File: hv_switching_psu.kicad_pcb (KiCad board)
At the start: 2 copper layers, 53.3 x 85 mm, 22 parts, among them P1 CONN_2, P2 CONN_2, P3 CONN_2, P4 CONN_1, SW1 SWITCH_INV, T1 IRF644PBF, U1 MAX1771

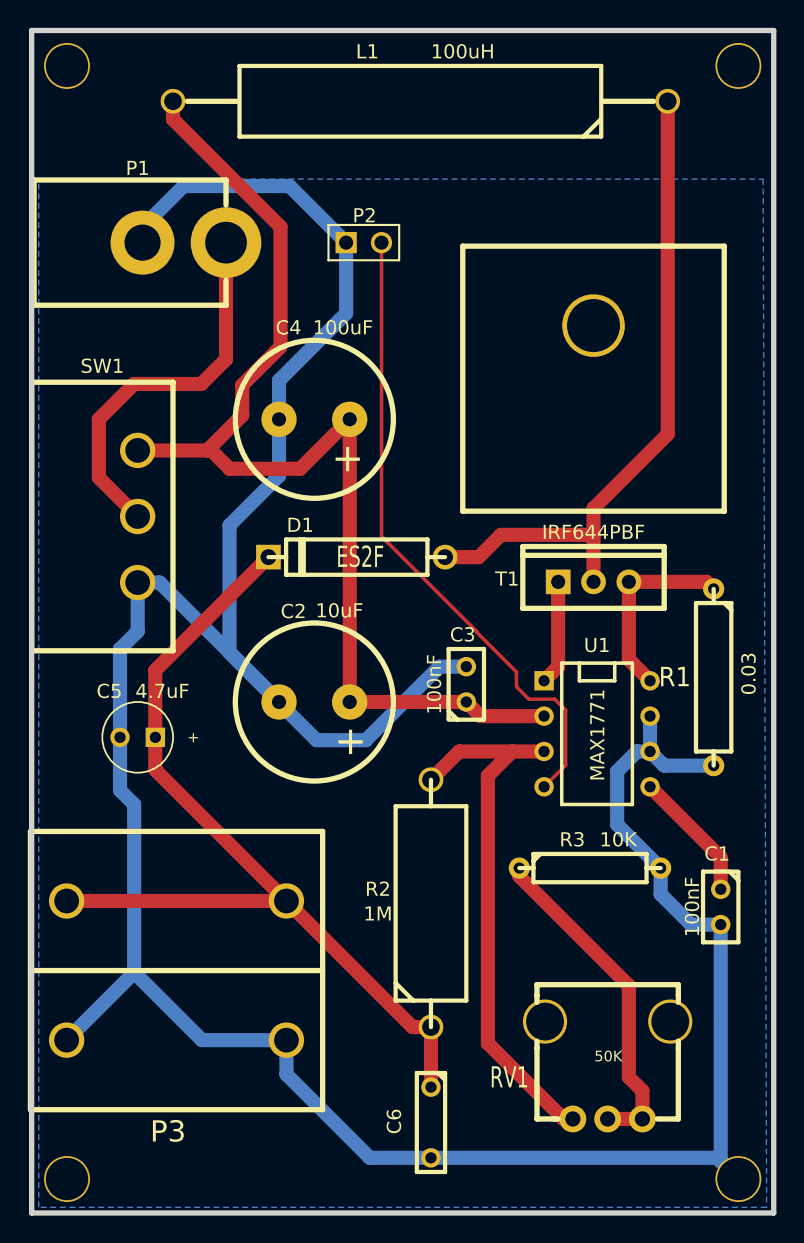
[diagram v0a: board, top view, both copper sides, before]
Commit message: Modified resistor settings.
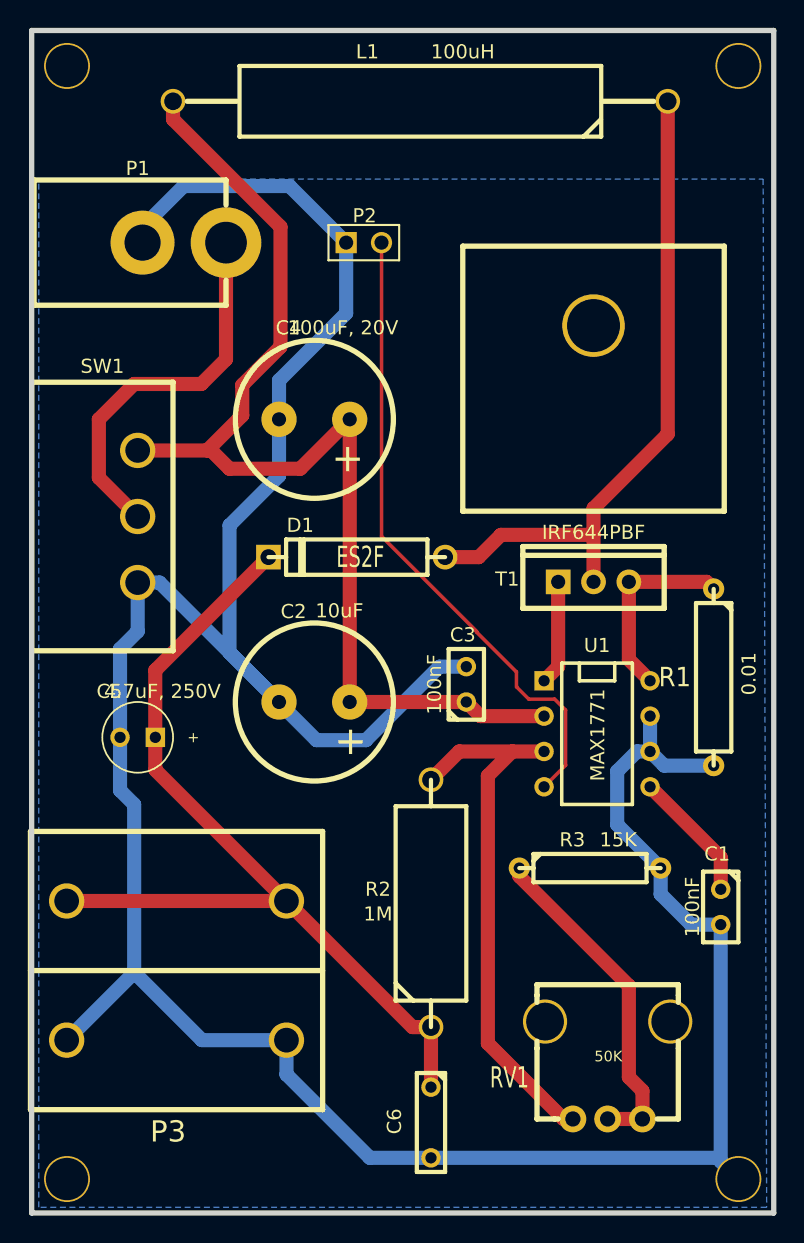
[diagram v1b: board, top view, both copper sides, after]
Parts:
- C4: value 100uF -> 100uF, 20V
- C5: value 4.7uF -> 4.7uF, 250V
- R1: value 0.03 -> 0.01
- R3: value 10K -> 15K
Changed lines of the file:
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@@
       (effects (font (size 1.016 1.016) (thickness 0.2032)))
     )
-    (fp_text value 100uF (at -2.0574 6.5786 180) (layer F.SilkS)
+    (fp_text value "100uF, 20V" (at -2.0574 6.5786 180) (layer F.SilkS)
       (effects (font (size 1.016 1.016) (thickness 0.2032)))
     )
@@
       (effects (font (size 1.016 1.016) (thickness 0.2032)))
     )
-    (fp_text value 4.7uF (at -1.778 3.302 180) (layer F.SilkS)
+    (fp_text value "4.7uF, 250V" (at -1.778 3.302 180) (layer F.SilkS)
       (effects (font (size 1.016 1.016) (thickness 0.2032)))
     )
@@
       (effects (font (size 1.016 1.016) (thickness 0.2032)))
     )
-    (fp_text value 10K (at 2.032 -2.032) (layer F.SilkS)
+    (fp_text value 15K (at 2.032 -2.032) (layer F.SilkS)
       (effects (font (size 1.016 1.016) (thickness 0.2032)))
     )
@@
       (effects (font (size 1.397 1.27) (thickness 0.2032)))
     )
-    (fp_text value 0.03 (at -0.254 -2.54 270) (layer F.SilkS)
-      (effects (font (size 1.016 1.016) (thickness 0.2032)))
-    )
+    (fp_text value 0.01 (at -0.254 -2.54 270) (layer F.SilkS)
+      (effects (font (size 1.016 1.016) (thickness 0.2032)))
+    )

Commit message: Added version 1.3 Gerber files.
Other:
- board text added: "IO Rodeo Inc. Electrophoresis Power Supply v 1.3"
- board text removed: "IO Rodeo Inc. Electrophoresis Power Supply v 1.2"
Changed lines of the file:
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@@
       (drillshape 0)
       (scaleselection 1)
-      (outputdirectory gerber_v1.2/))
+      (outputdirectory gerber_v1.3/))
   )
   (net 0 "")
@@
   (gr_line (start 139.7 165) (end 86.36 165) (angle 90) (layer Edge.Cuts) (width 0.381))
   (gr_line (start 86.36 80) (end 139.7 80) (angle 90) (layer Edge.Cuts) (width 0.381))
-  (gr_text "IO Rodeo Inc.\nElectrophoresis Power Supply v 1.2" (at 114.554 83.312) (layer B.SilkS)
+  (gr_text "IO Rodeo Inc.\nElectrophoresis Power Supply v 1.3" (at 114.554 83.312) (layer B.SilkS)
     (effects (font (size 1.524 1.016) (thickness 0.254)) (justify mirror))
   )

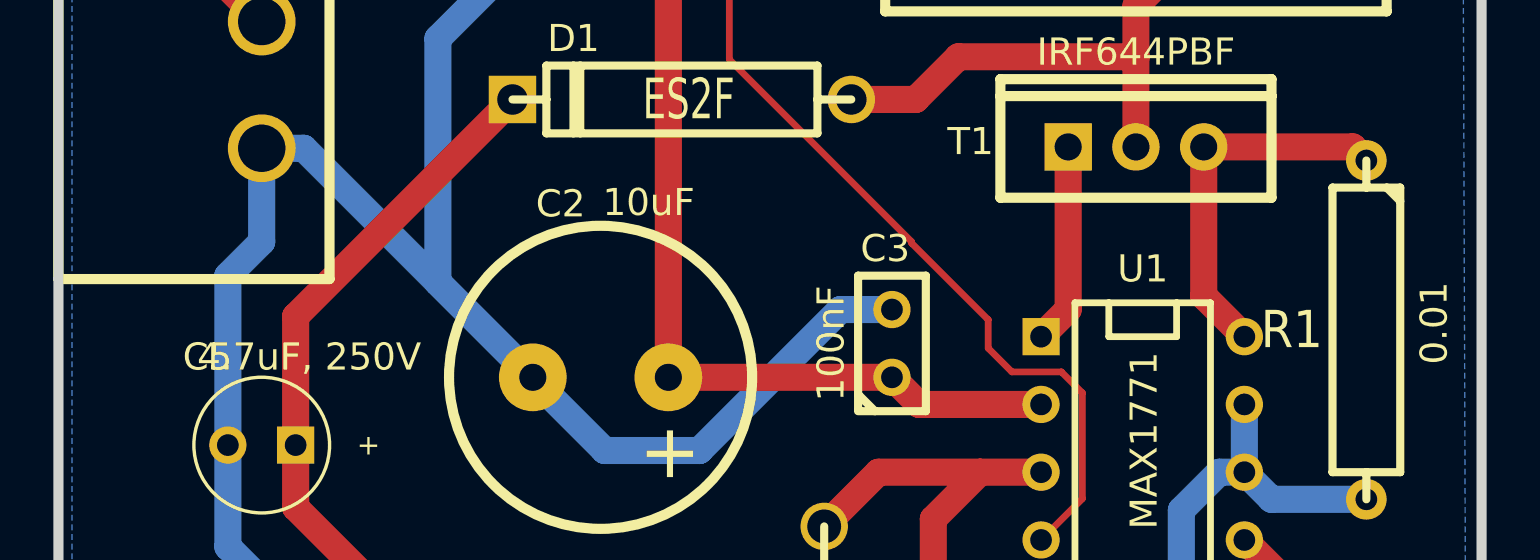
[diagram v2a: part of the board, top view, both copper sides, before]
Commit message: Modified silkscreen, remade v1.3 of gerber files.
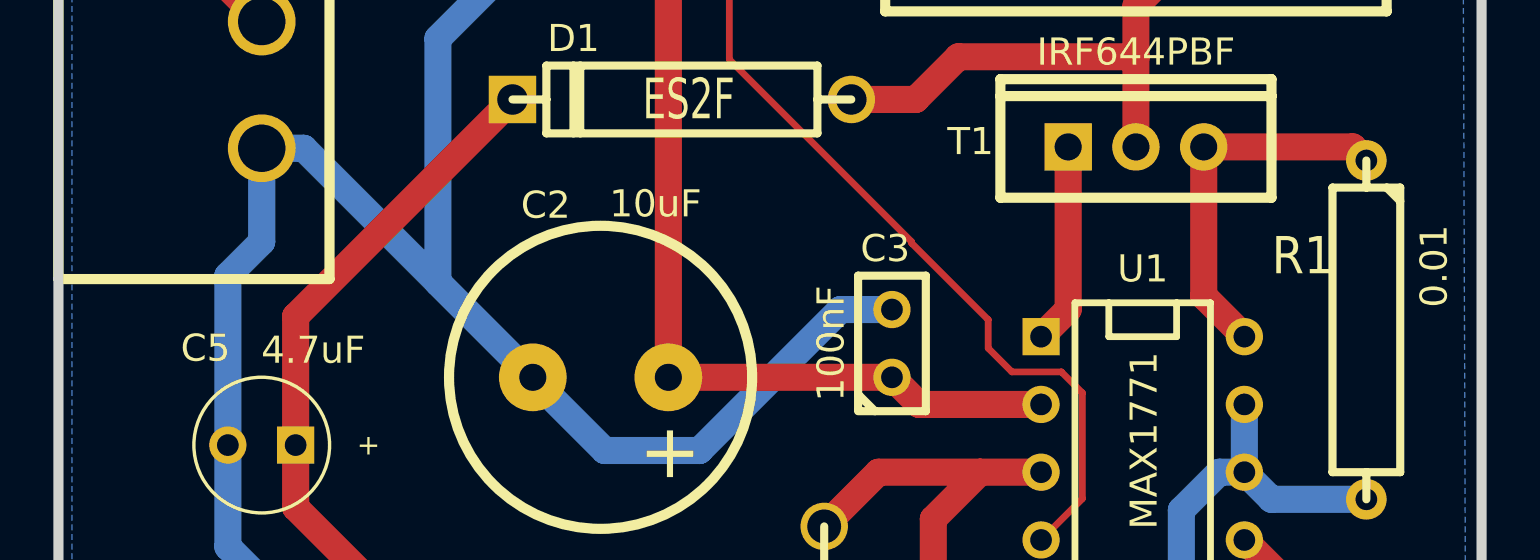
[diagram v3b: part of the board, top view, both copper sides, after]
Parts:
- C5: value 4.7uF, 250V -> 4.7uF
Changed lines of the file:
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@@
   (module CAPPOL (layer Front)
     (at 106.68 128.27 180)
-    (fp_text reference C2 (at 1.4986 6.5024 180) (layer F.SilkS)
-      (effects (font (size 1.016 1.016) (thickness 0.2032)))
-    )
-    (fp_text value 10uF (at -1.8034 6.5532 180) (layer F.SilkS)
+    (fp_text reference C2 (at 2.0574 6.4516 180) (layer F.SilkS)
+      (effects (font (size 1.016 1.016) (thickness 0.2032)))
+    )
+    (fp_text value 10uF (at -2.0574 6.5024 180) (layer F.SilkS)
       (effects (font (size 1.016 1.016) (thickness 0.2032)))
     )
@@
     (descr "Condensateur e = 1 pas")
     (tags C)
-    (fp_text reference C5 (at 2.032 3.302 180) (layer F.SilkS)
-      (effects (font (size 1.016 1.016) (thickness 0.2032)))
-    )
-    (fp_text value "4.7uF, 250V" (at -1.778 3.302 180) (layer F.SilkS)
+    (fp_text reference C5 (at 2.1082 3.6322 180) (layer F.SilkS)
+      (effects (font (size 1.016 1.016) (thickness 0.2032)))
+    )
+    (fp_text value 4.7uF (at -1.9304 3.556 180) (layer F.SilkS)
       (effects (font (size 1.016 1.016) (thickness 0.2032)))
     )
@@
     (tags R)
     (autoplace_cost180 10)
-    (fp_text reference R1 (at 0 2.794 360) (layer F.SilkS)
+    (fp_text reference R1 (at -2.7686 2.3876 360) (layer F.SilkS)
       (effects (font (size 1.397 1.27) (thickness 0.2032)))
     )
-    (fp_text value 0.01 (at -0.254 -2.54 270) (layer F.SilkS)
-      (effects (font (size 1.016 1.016) (thickness 0.2032)))
-    )
+    (fp_text value 0.01 (at -2.3876 -2.54 270) (layer F.SilkS)
+      (effects (font (size 1.016 1.016) (thickness 0.2032)))
+    )

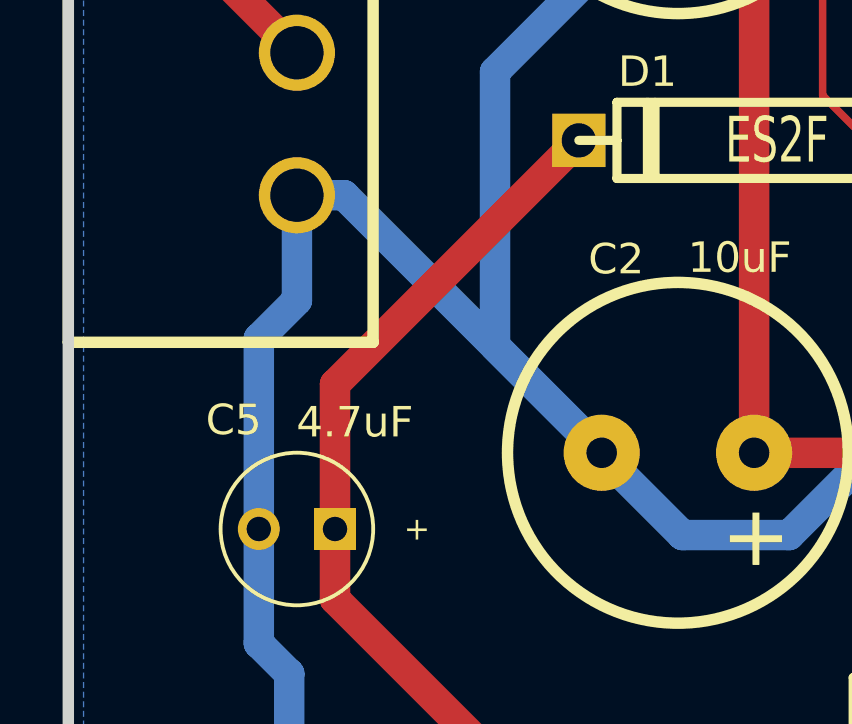
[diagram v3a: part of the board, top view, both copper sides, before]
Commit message: Added version 1.4 of design - fixed issue with switch.
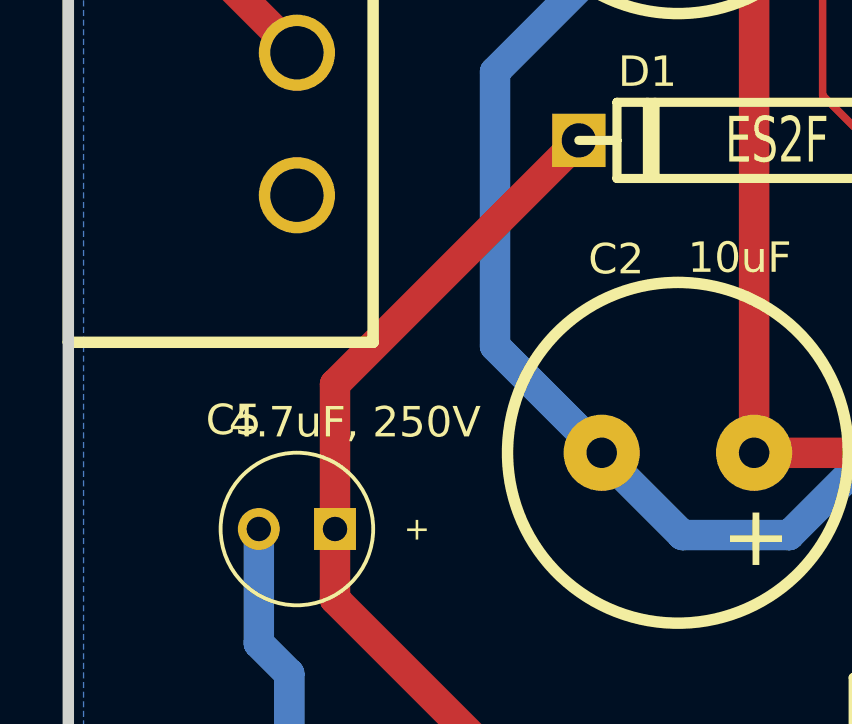
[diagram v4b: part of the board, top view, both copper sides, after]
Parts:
- C5: value 4.7uF -> 4.7uF, 250V
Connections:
- SW1 pad 3: GND -> (no net)
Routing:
- net GND: track 218.7 -> 193.3 mm
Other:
- board text added: "IO Rodeo Inc. Electrophoresis Power Supply v 1.4"
- board text removed: "IO Rodeo Inc. Electrophoresis Power Supply v 1.3"
